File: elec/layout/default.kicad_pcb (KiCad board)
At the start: 2 copper layers, 57 x 4 mm, 14 parts, among them J1 Power_Connector, J2 Power_Connector, J3 LED_Connector, J4 LED_Connector, J5 USB_Type_C_Receptacle_16_pin, K1 Relay, U1 WCHJiangsu_Qin_Heng_CH224K

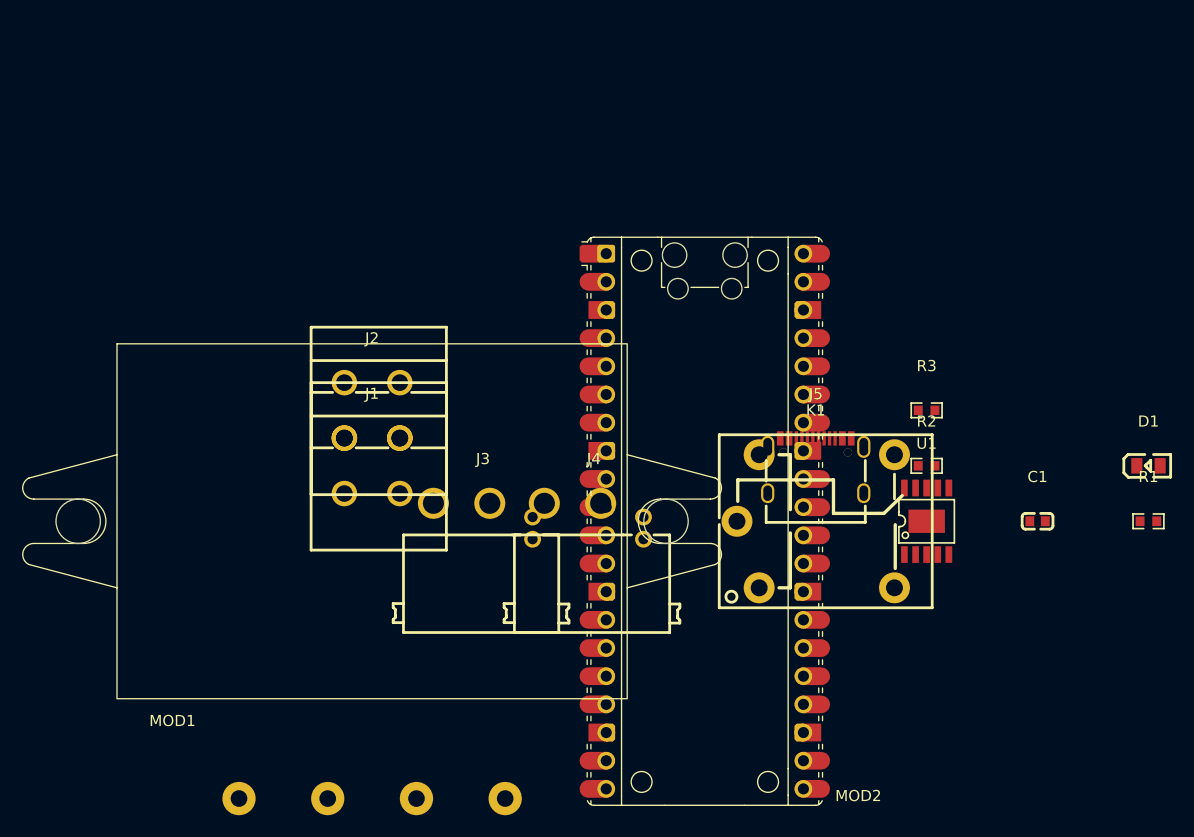
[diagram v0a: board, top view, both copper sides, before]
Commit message: Split into modules, and add first layout
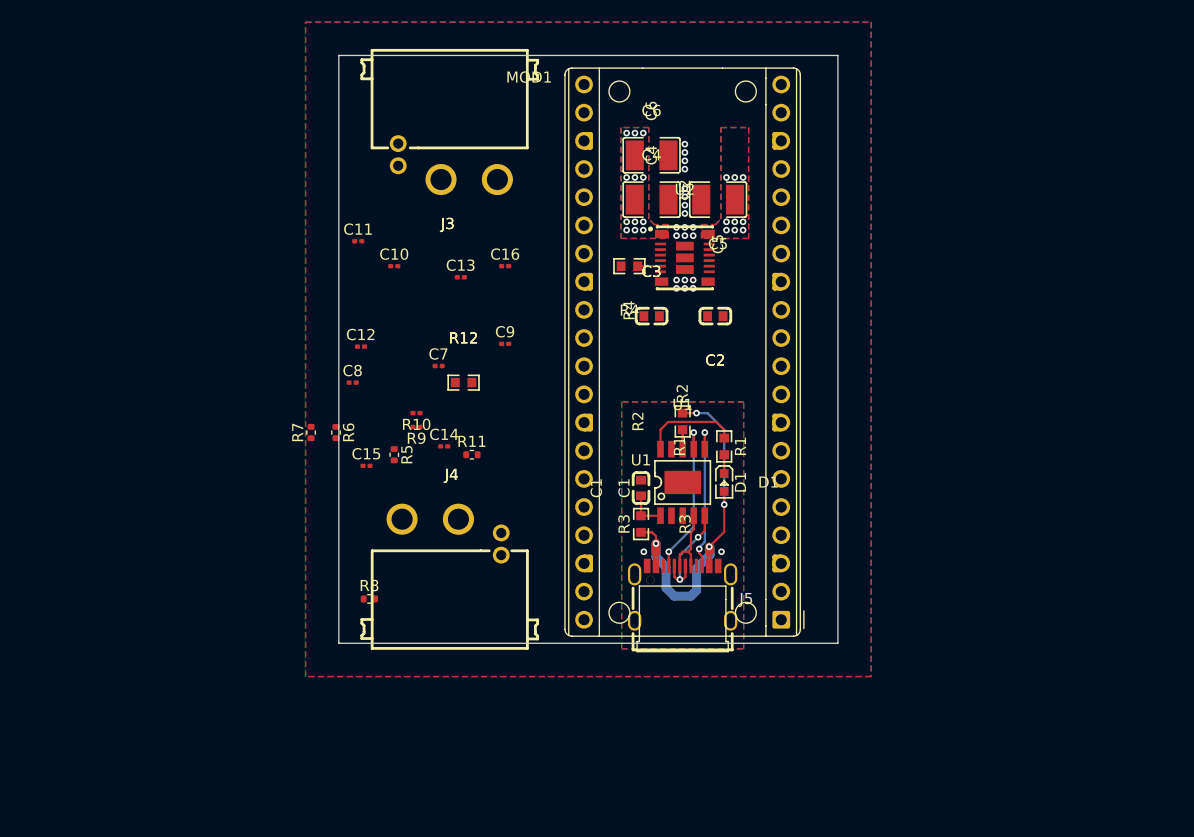
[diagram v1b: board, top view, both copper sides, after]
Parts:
- removed J1, J2: Power_Connector, lcsc:CONN-TH_P5.00_KF243-5.0-2P
- removed K1: Relay, lcsc:RELAY-TH_SRD-XXVDC-XL-C
- removed MOD2: RaspberryPiPico, ki-lime-pi-pico:RaspberryPi_Pico_Common
- added C10: , atopile:C_0201_0603Metric, F.Cu at (2.00, -23.0)
- added C11: , atopile:C_0201_0603Metric, F.Cu at (-1.25, -25.2)
- added C12: , atopile:C_0201_0603Metric, F.Cu at (-1.00, -15.8)
- added C13: , atopile:C_0201_0603Metric, F.Cu at (8.00, -22.0)
- added C14: , atopile:C_0201_0603Metric, F.Cu at (6.50, -6.75)
- added C15: , atopile:C_0201_0603Metric, F.Cu at (-0.50, -5.00)
- added C16: , atopile:C_0201_0603Metric, F.Cu at (12.0, -23.0)
- added C2: 10µF ±10% 10V X5R, atopile:C0603-bd72f6, F.Cu at (30.9, -18.5)
- added C3: 10µF ±10% 10V X5R, atopile:C0603-bd72f6, F.Cu at (25.2, -18.5)
- added C4: 22µF ±10% 25V X7R, atopile:C1210-c93926, F.Cu at (25.2, -29.0)
- added C5: 22µF ±10% 25V X7R, atopile:C1210-c93926, F.Cu at (31.2, -29.0)
- added C6: 22µF ±10% 25V X7R, atopile:C1210-c93926, F.Cu at (25.2, -33.0)
- added C7: , atopile:C_0201_0603Metric, F.Cu at (6.00, -14.0)
- added C8: , atopile:C_0201_0603Metric, F.Cu at (-1.75, -12.5)
- added C9: , atopile:C_0201_0603Metric, F.Cu at (12.0, -16.0)
- added R10: , atopile:R_0201_0603Metric, F.Cu at (4.00, -9.75)
- added R11: , atopile:R_0402_1005Metric, F.Cu at (9.00, -6.00)
- added R12: 162kΩ ±1% 100mW, atopile:R0603-ebcab9, F.Cu at (8.25, -12.5)
- added R4: 100kΩ ±1% 100mW, atopile:R0603-ebcab9, F.Cu at (23.2, -23.0)
- added R5: , atopile:R_0402_1005Metric, F.Cu at (2.00, -6.00)
- added R6: , atopile:R_0402_1005Metric, F.Cu at (-3.25, -8.00)
- added R7: , atopile:R_0402_1005Metric, F.Cu at (-5.50, -8.00)
- added R8: , atopile:R_0402_1005Metric, F.Cu at (-0.25, 7.00)
- added R9: , atopile:R_0201_0603Metric, F.Cu at (4.00, -8.50)
- added U2: , atopile:B3QFN-19_L5.5-W5.0-P0.50-TL-114622, F.Cu at (28.2, -23.8)
- C1: footprint lcsc:C0603 -> atopile:C0603-bd72f6
- D1: footprint lcsc:LED0805-R-RD -> atopile:LED0603-RD-YELLOW-5af84a
- J3, J4: value LED_Connector -> (none); footprint lcsc:CONN-TH_4P-XT30PW-M -> atopile:CONN-TH_4P-XT30PW-M-e6a65c
- J5: value USB_Type_C_Receptacle_16_pin -> (none); footprint lcsc:USB-C_SMD-TYPE-C-31-M-12 -> atopile:USB-C_SMD-TYPE-C-31-M-12-8412ae
- MOD1: value DCDC_Converter -> (none); footprint custom:DCDC_Module -> ki-lime-pi-pico:RaspberryPi_Pico_Common_THT
- R1, R2, R3: footprint lcsc:R0603 -> atopile:R0603-ebcab9
- U1: value WCHJiangsu_Qin_Heng_CH224K -> (none); footprint lcsc:ESSOP-10_L4.9-W3.9-P1.0-LS6.0-TL-EP -> atopile:ESSOP-10_L4.9-W3.9-P1.0-LS6.0-TL-EP-20a8ca
- moved R1 38.8 mm to (31.8, -6.75), turned to 90 degrees
- moved D1 38.3 mm to (31.8, -3.50), turned to -90 degrees
- moved C1 35.9 mm to (24.2, -3.00), turned to 90 degrees
- moved J3 32.6 mm to (6.83, -32.4), turned to 180 degrees
- moved MOD1 31.9 mm to (28.0, -15.2), turned to 180 degrees
- moved R3 27.7 mm to (24.2, 0.25), turned to -90 degrees
- moved R2 22.4 mm to (28.0, -9.00), turned to 90 degrees
- moved U1 22.3 mm to (28.0, -3.50)
- moved J5 16.6 mm to (28.0, 6.50)
- moved J4 12.9 mm to (7.17, 1.43)
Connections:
- net dcdc_module.dcdc_converter.footprint.pins[0].net-net renamed mcu-contact[0]
- net dcdc_module.dcdc_converter.footprint.pins[1].net-net renamed mcu-contact[1]
- net pd_power_supply.usb_pr_trigger-gnd renamed pd_power_supply-gnd
- C1 pad 2: gnd -> gnd-2
- D1 pad 1: pd_power_supply-hv -> pd_power_supply.usb_pr_trigger.power_good_indicator.led-cathode
- D1 pad 2: cathode -> vbus
- J3 pad 1: hv -> hv-1
- J3 pad 2: gnd-1 -> gnd-2
- J3 pad 3: signal-1 -> data
- J3 pad 4: signal -> clock
- J4 pad 1: hv -> hv-1
- J4 pad 2: gnd-1 -> gnd-2
- J4 pad 3: signal -> clock
- J4 pad 4: signal-1 -> data
- J5 pad A1: gnd -> gnd-2
- J5 pad A12: gnd -> gnd-2
- J5 pad A4: pd_power_supply-hv -> vbus
- J5 pad A6: pd_power_supply-signal -> pd_power_supply-signal-1
- J5 pad A7: pd_power_supply-signal-1 -> pd_power_supply-signal
- J5 pad A9: pd_power_supply-hv -> vbus
- J5 pad B1: gnd -> gnd-2
- J5 pad B12: gnd -> gnd-2
- J5 pad B4: pd_power_supply-hv -> vbus
- J5 pad B6: pd_power_supply-signal -> pd_power_supply-signal-1
- J5 pad B7: pd_power_supply-signal-1 -> pd_power_supply-signal
- J5 pad B9: pd_power_supply-hv -> vbus
- MOD1 pad 3: dcdc_module.dcdc_converter.footprint.pins[2].net-net -> mcu.base.decoupling_power_io_specialized.capacitors[0].footprint.pins[2].net-net
- MOD1 pad 4: dcdc_module.dcdc_converter.footprint.pins[3].net-net -> clock
- R1 pad 1: cathode -> pd_power_supply.usb_pr_trigger.power_good_indicator.led-cathode
- R2 pad 2: pd_power_supply-hv -> vbus
- R3 pad 2: pd_power_supply-hv -> vbus
- U1 pad 11: gnd -> gnd-2
- U1 pad 2: pd_power_supply.usb_pr_trigger.controller-signal-1 -> pd_power_supply.usb_pr_trigger.controller-signal
- U1 pad 3: pd_power_supply.usb_pr_trigger.controller-signal -> pd_power_supply.usb_pr_trigger.controller-signal-2
- U1 pad 4: pd_power_supply-signal -> pd_power_supply-signal-1
- U1 pad 5: pd_power_supply-signal-1 -> pd_power_supply-signal
- U1 pad 9: pd_power_supply.usb_pr_trigger.controller-signal-2 -> pd_power_supply.usb_pr_trigger.controller-signal-1
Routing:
- net vbus: track 0.00 -> 37.3 mm, vias 0 -> 4
- net cc[0]: track 0.00 -> 14.5 mm, vias 0 -> 2
- net cc[1]: track 0.00 -> 13.8 mm, vias 0 -> 2
- net pd_power_supply-signal: track 0.00 -> 9.83 mm, vias 0 -> 2
- net pd_power_supply-gnd: track 0.00 -> 8.83 mm
- net pd_power_supply-signal-1: track 0.00 -> 6.72 mm
- net pd_power_supply.usb_pr_trigger-hv: track 0.00 -> 3.55 mm
- net dcdc_module-signal: track 0.00 -> 2.05 mm
- net pd_power_supply.usb_pr_trigger-signal: track 0.00 -> 1.75 mm
- net pd_power_supply.usb_pr_trigger.power_good_indicator.led-cathode: track 0.00 -> 1.70 mm
- net sbu2: vias 0 -> 2
- net mcu.base.decoupling_power_io_specialized.capacitors[0].footprint.pins[2].net-net: vias 0 -> 3
- net hv-1: vias 0 -> 21
- net (no net): vias 0 -> 17
- added copper zone on B.Cu, net gnd-2
- added copper zone on F.Cu, net gnd-2
- added copper zone on B.Cu, net hv-1
- added copper zone on F.Cu, net hv-1
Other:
- board size 57 x 4 mm -> 45 x 53 mm

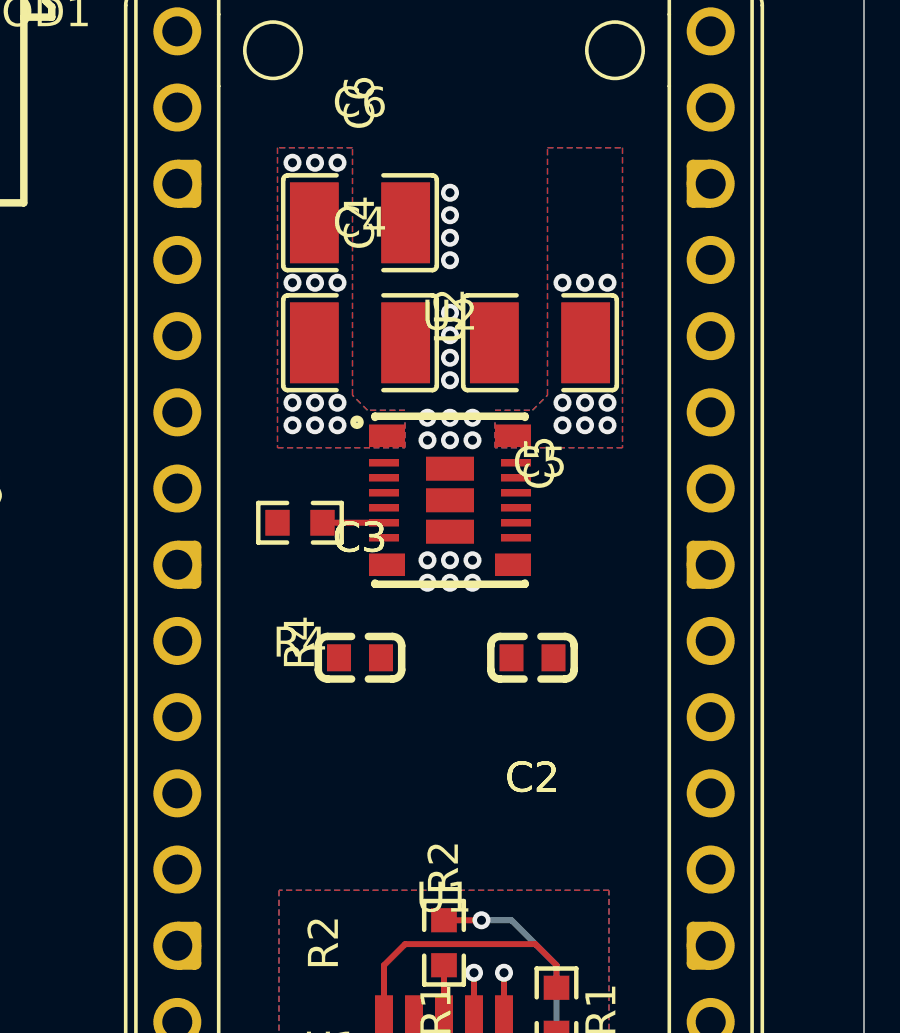
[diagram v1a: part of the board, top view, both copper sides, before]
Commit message: Change PCB layout
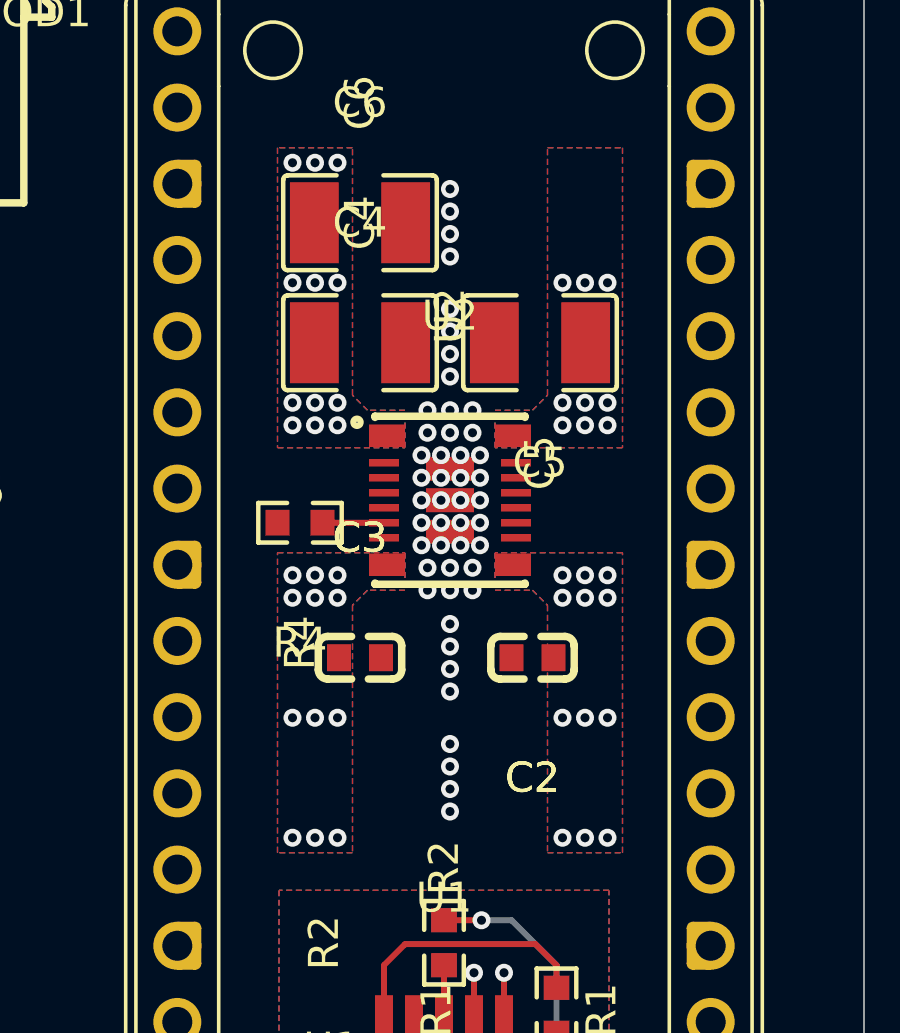
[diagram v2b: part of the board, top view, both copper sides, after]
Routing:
- net vbus: vias 4 -> 28
- net sbu2: vias 2 -> 0
- net mcu.base.decoupling_power_io_specialized.capacitors[0].footprint.pins[2].net-net: vias 3 -> 0
- net mcu-contact[6]: vias 0 -> 2
- net gnd-2: vias 0 -> 22
- net contact[13]: vias 0 -> 4
- net (no net): vias 17 -> 22
- added copper zone on B.Cu, net vbus
- added copper zone on F.Cu, net vbus

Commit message: Add LED buffer, change DCDC func to params, layout
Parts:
- added C17: 10nF ±1% 50V C0G, atopile:C0805-3b2e55, F.Cu at (400.0, -5.00)
- added C18: 22nF ±1% 50V, atopile:C0805-3b2e55, F.Cu at (370.0, -5.00)
- added R13: 49.9Ω ±1% 100mW, atopile:R0603-ebcab9, F.Cu at (190.0, -5.00)
- added R14: 0Ω 100mW, atopile:R0603-ebcab9, F.Cu at (110.0, -5.00)
- added R15: 162kΩ ±1% 100mW, atopile:R0603-ebcab9, F.Cu at (20.0, -5.00)
- C1: value 100nF ±10% 50V X7R -> 1µF ±10% 50V X5R
- R12: value 162kΩ ±1% 100mW -> 10kΩ ±1% 100mW
- moved R12 201.9 mm to (210.0, -5.00)
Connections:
- net contact[18] renamed mcu-contact[18]-1
- net dcdc_module-signal renamed dcdc_module-line
- net dcdc_module-signal-1 renamed dcdc_module-line-1
- net gnd-2 renamed gnd-1
- net mcu-contact[19] renamed mcu-contact[18]
- net mcu-contact[19]-1 renamed contact[19]
- net mcu-signal renamed mcu-line
- net mcu-signal-1 renamed mcu-line-1
- net mcu-signal-2 renamed mcu-line-2
- net mcu.base-signal-1 renamed mcu.base.runtime_anon[0].runtime_anon[1].footprint.pins[1].net-net
- net mcu.base-signal-4 renamed mcu.base.runtime_anon[0].runtime_anon[0].footprint.pins[1].net-net
- net mcu.base-signal-5 renamed mcu.base-line-4
- net mcu.base.runtime_anon[0].runtime_anon[0].footprint.pins[2].net-net renamed mcu.base-line
- net mcu.base.runtime_anon[0].runtime_anon[1].footprint.pins[2].net-net renamed mcu.base-line-1
- net pd_power_supply-signal renamed pd_power_supply-line
- net pd_power_supply-signal-1 renamed pd_power_supply-line-1
- net pd_power_supply.usb_pr_trigger-signal renamed pd_power_supply.usb_pr_trigger-line
- net pd_power_supply.usb_pr_trigger.controller-signal renamed pd_power_supply.usb_pr_trigger.controller-line-1
- net pd_power_supply.usb_pr_trigger.controller-signal-1 renamed pd_power_supply.usb_pr_trigger.controller-line
- net pd_power_supply.usb_pr_trigger.controller-signal-2 renamed pd_power_supply.usb_pr_trigger.controller-line-2
- C10 pad : (no net) -> hv
- C10 pad 1: mcu.base.decoupling_power_io_specialized.capacitors[0].footprint.pins[2].net-net -> gnd
- C10 pad 2: mcu.base.decoupling_power_io_specialized.capacitors[0].footprint.pins[2].net-net -> mcu.base.decoupling_power_usb_phy.footprint.pins[2].net-net
- C11 pad : (no net) -> hv
- C11 pad 1: mcu.base.decoupling_power_io_specialized.capacitors[0].footprint.pins[2].net-net -> gnd
- C12 pad : (no net) -> hv
- C12 pad 1: mcu.base.decoupling_power_io_specialized.capacitors[3].footprint.pins[2].net-net -> gnd
- C12 pad 2: mcu.base.decoupling_power_io_specialized.capacitors[0].footprint.pins[2].net-net -> mcu.base.decoupling_power_usb_phy.footprint.pins[2].net-net
- C13 pad : (no net) -> hv
- C13 pad 1: mcu.base.decoupling_power_io_specialized.capacitors[0].footprint.pins[2].net-net -> mcu.base.decoupling_power_usb_phy.footprint.pins[2].net-net
- C13 pad 2: mcu.base.decoupling_power_io_specialized.capacitors[3].footprint.pins[2].net-net -> gnd
- C14 pad : (no net) -> hv
- C14 pad 1: mcu.base.decoupling_power_io_specialized.capacitors[0].footprint.pins[2].net-net -> gnd
- C14 pad 2: mcu.base.decoupling_power_io_specialized.capacitors[0].footprint.pins[2].net-net -> mcu.base.decoupling_power_usb_phy.footprint.pins[2].net-net
- C15 pad : (no net) -> hv
- C15 pad 1: mcu.base.decoupling_power_io_specialized.capacitors[0].footprint.pins[2].net-net -> mcu.base.decoupling_power_usb_phy.footprint.pins[2].net-net
- C15 pad 2: mcu.base.decoupling_power_io_specialized.capacitors[5].footprint.pins[2].net-net -> gnd
- C16 pad : (no net) -> hv
- C16 pad 1: mcu.base.decoupling_power_io_specialized.capacitors[0].footprint.pins[2].net-net -> gnd
- C16 pad 2: mcu.base.decoupling_power_io_specialized.capacitors[0].footprint.pins[2].net-net -> mcu.base.decoupling_power_usb_phy.footprint.pins[2].net-net
- C7 pad : (no net) -> mcu.base-line-2
- C7 pad 1: mcu.base.decoupling_power_io_specialized.capacitors[5].footprint.pins[2].net-net -> mcu.base.decoupling_power_adc.footprint.pins[1].net-net
- C7 pad 2: mcu.base.decoupling_power_io_specialized.capacitors[0].footprint.pins[2].net-net -> gnd
- C8 pad : (no net) -> mcu.base-hv
- C8 pad 1: mcu.base.decoupling_power_io_specialized.capacitors[0].footprint.pins[2].net-net -> gnd
- C8 pad 2: mcu.base.decoupling_power_io_specialized.capacitors[0].footprint.pins[2].net-net -> mcu.base.decoupling_power_usb_phy.footprint.pins[2].net-net
- C9 pad : (no net) -> mcu.base-hv
- C9 pad 1: mcu.base.decoupling_power_io_specialized.capacitors[0].footprint.pins[2].net-net -> mcu.base.decoupling_power_usb_phy.footprint.pins[2].net-net
- C9 pad 2: mcu.base.decoupling_power_core_specialized.capacitors[1].footprint.pins[2].net-net -> gnd
- MOD1 pad 10: mcu-contact[9] -> mcu-contact[9]-1
- MOD1 pad 13: mcu.base.decoupling_power_io_specialized.capacitors[0].footprint.pins[2].net-net -> gnd
- MOD1 pad 15: mcu-contact[14]-1 -> mcu-contact[14]
- MOD1 pad 18: mcu.base.decoupling_power_io_specialized.capacitors[0].footprint.pins[2].net-net -> gnd
- MOD1 pad 2: mcu-contact[1] -> mcu-contact[1]-1
- MOD1 pad 22: mcu-contact[1]-1 -> mcu-contact[1]
- MOD1 pad 23: mcu.base.decoupling_power_io_specialized.capacitors[0].footprint.pins[2].net-net -> gnd
- MOD1 pad 27: mcu-contact[6] -> mcu-contact[6]-1
- MOD1 pad 28: mcu.base.decoupling_power_io_specialized.capacitors[0].footprint.pins[2].net-net -> gnd
- MOD1 pad 3: mcu.base.decoupling_power_io_specialized.capacitors[0].footprint.pins[2].net-net -> gnd
- MOD1 pad 30: mcu-contact[9]-1 -> mcu-contact[9]
- MOD1 pad 33: mcu.base.decoupling_power_io_specialized.capacitors[0].footprint.pins[2].net-net -> gnd
- MOD1 pad 35: mcu-contact[14] -> mcu-contact[14]-1
- MOD1 pad 36: hv-2 -> hv
- MOD1 pad 38: mcu.base.decoupling_power_io_specialized.capacitors[0].footprint.pins[2].net-net -> gnd
- MOD1 pad 7: mcu-contact[6]-1 -> mcu-contact[6]
- MOD1 pad 8: mcu.base.decoupling_power_io_specialized.capacitors[0].footprint.pins[2].net-net -> gnd
- R10 pad : (no net) -> mcu.base-line-5
- R11 pad 2: mcu.base.decoupling_power_io_specialized.capacitors[0].footprint.pins[2].net-net -> gnd
- R12 pad 1: frequency_mode -> feedback
- R12 pad 2: gnd -> dcdc_module-gnd
- R5 pad 1: hv-2 -> hv
- R5 pad 2: mcu.base-signal-2 -> mcu.base-line-2
- R6 pad 2: hv-2 -> hv
- R9 pad : (no net) -> mcu.base-line-3
- U2 pad 5: gnd -> dcdc_module-gnd
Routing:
- net mcu-contact[6]-1: vias 0 -> 2
- net mcu-contact[6]: vias 2 -> 0
